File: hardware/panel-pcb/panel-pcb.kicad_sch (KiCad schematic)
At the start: 134 parts, among them J1 USB_C_Receptacle_USB2.0_16P, J10 RS-485 OUT, J11 12V_OUT, J2 SWD, J3 FSR North, J4 FSR East, J5 12V_IN, J6 FSR South, J7 FSR West, J8 RS-485 IN, J9 INT OUT, SW1 PANEL_ID, SW2 BOOTSEL, SW3 RS-485 Termination, U1 RP2040, U2 THVD1419, U3 W25Q32JV, U4 SN74AHCT125, U5 AMS1117-5.0, U6 AP7361C-33ER-13, U7 USBLC6-2SC6, X1 12MHz ABM8-272-T3

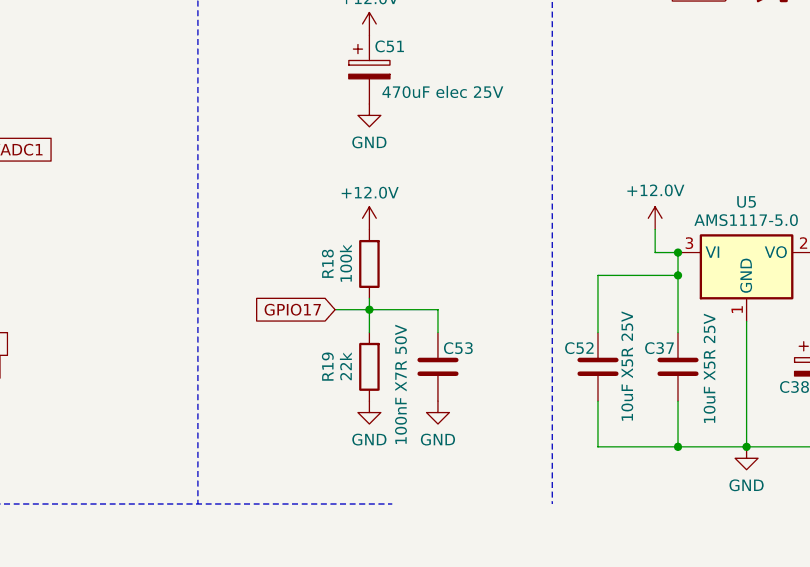
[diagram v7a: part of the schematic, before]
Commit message: Panel PCB: board art, name/rev silk, follow-up review fixes
- Silkscreen: 'Kraken Pad by SenPi / Rev. 1.0' (F.Silk), JLC order-number
  placeholder JLCJLCJLCJLC (B.Silk).
- Personal logo as exposed copper: 5 poly pairs F.Cu + point-registered
  F.Mask openings; degenerate near-zero-area sliver pair deleted
  (follow-up review F3).
- R19 22k -> 33k: 12V-sense node ~2.98V, ~1V margin over guaranteed
  2.0V VIH (follow-up review F1; old 22k value had 164mV nominal margin).
- New D29 PMEG3015EH clamp, anode GPIO17 / cathode +3V3: bounds the
  sense node to one Vf above the rail when IOVDD is down, closing the
  RP2040 abs-max-vs-FT-description ambiguity (follow-up review F2).
- Via DRC rules switched to JLC 4-layer standard class (0.3mm drill /
  0.45mm dia) - board passes clean, no premium via process needed.

ERC: 1 warning (D29 cached D_Schottky lib_symbol_mismatch, known noise
class). DRC 0 violations, 0 unconnected.
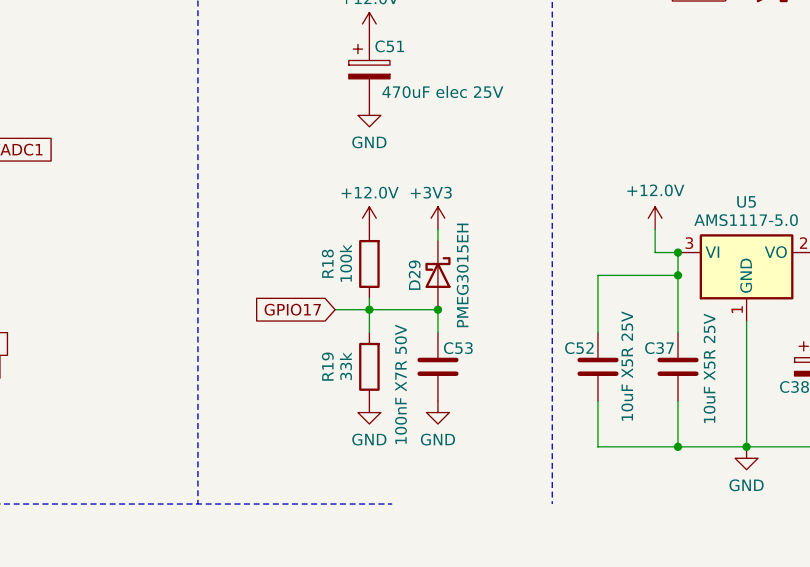
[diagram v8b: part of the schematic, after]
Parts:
- added D29: PMEG3015EH, Diode_SMD:D_SOD-123F, symbol Device:D_Schottky
- R19: value 22k -> 33k
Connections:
- net +3V3: now also D29.1 (K)
- net GPIO17: now also D29.2 (A)
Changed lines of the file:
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@@
 	)
 	(junction
+		(at 304.8 231.14)
+		(diameter 0)
+		(color 0 0 0 0)
+	)
+	(junction
 		(at 92.71 137.16)
 		(diameter 0)
@@
 	(wire
 		(pts
+			(xy 304.8 222.25) (xy 304.8 223.52)
+		)
+		(stroke
+			(width 0)
+			(type default)
+		)
+	)
+	(wire
+		(pts
 			(xy 49.53 138.43) (xy 41.91 138.43)
 		)
@@
 	(symbol
 		(lib_id "power:+3V3")
+		(at 304.8 222.25 0)
+		(unit 1)
+		(body_style 1)
+		(exclude_from_sim no)
+		(in_bom yes)
+		(on_board yes)
+		(in_pos_files yes)
+		(dnp no)
+		(property "Reference" "#PWR0158"
+			(at 304.8 218.44 0)
+			(hide yes)
+			(show_name no)
+			(do_not_autoplace no)
+			(effects
+				(font
+					(size 1.27 1.27)
+				)
+			)
+		)
+		(property "Value" "+3V3"
+			(at 304.038 218.186 0)
+			(show_name no)
+			(do_not_autoplace no)
+			(effects
+				(font
+					(size 1.27 1.27)
+				)
+			)
+		)
+		(property "Footprint" ""
+			(at 304.8 222.25 0)
+			(hide yes)
+			(show_name no)
+			(do_not_autoplace no)
+			(effects
+				(font
+					(size 1.27 1.27)
+				)
+			)
+		)
+		(property "Datasheet" ""
+			(at 304.8 222.25 0)
+			(hide yes)
+			(show_name no)
+			(do_not_autoplace no)
+			(effects
+				(font
+					(size 1.27 1.27)
+				)
+			)
+		)
+		(property "Description" ""
+			(at 304.8 222.25 0)
+			(hide yes)
+			(show_name no)
+			(do_not_autoplace no)
+			(effects
+				(font
+					(size 1.27 1.27)
+				)
+			)
+		)
+		(pin "1"
+		)
+		(instances
+			(project "panel-pcb"
+				(path "/a1b2c3d4-0000-4000-8000-000000000001"
+					(reference "#PWR0158")
+					(unit 1)
+				)
+			)
+		)
+	)
+	(symbol
+		(lib_id "power:+3V3")
 		(at 309.88 31.75 0)
 		(unit 1)
@@
 	)
 	(symbol
+		(lib_id "Device:D_Schottky")
+		(at 304.8 227.33 270)
+		(unit 1)
+		(body_style 1)
+		(exclude_from_sim no)
+		(in_bom yes)
+		(on_board yes)
+		(in_pos_files yes)
+		(dnp no)
+		(property "Reference" "D29"
+			(at 302.26 227.33 0)
+			(show_name no)
+			(do_not_autoplace no)
+			(effects
+				(font
+					(size 1.27 1.27)
+				)
+			)
+		)
+		(property "Value" "PMEG3015EH"
+			(at 307.594 227.33 0)
+			(show_name no)
+			(do_not_autoplace no)
+			(effects
+				(font
+					(size 1.27 1.27)
+				)
+			)
+		)
+		(property "Footprint" "Diode_SMD:D_SOD-123F"
+			(at 299.72 227.33 0)
+			(hide yes)
+			(show_name no)
+			(do_not_autoplace no)
+			(effects
+				(font
+					(size 1.27 1.27)
+				)
+			)
+		)
+		(property "Datasheet" "https://assets.nexperia.com/documents/data-sheet/PMEG3015EH.pdf"
+			(at 299.72 227.33 0)
+			(hide yes)
+			(show_name no)
+			(do_not_autoplace no)
+			(effects
+				(font
+					(size 1.27 1.27)
+				)
+			)
+		)
+		(property "Description" "GPIO17 12V-sense clamp to +3V3\""
+			(at 299.72 227.33 0)
+			(hide yes)
+			(show_name no)
+			(do_not_autoplace no)
+			(effects
+				(font
+					(size 1.27 1.27)
+				)
+			)
+		)
+		(pin "1"
+		)
+		(pin "2"
+		)
+		(instances
+			(project "panel-pcb"
+				(path "/a1b2c3d4-0000-4000-8000-000000000001"
+					(reference "D29")
+					(unit 1)
+				)
+			)
+		)
+	)
+	(symbol
 		(lib_id "Device:C")
 		(at 71.12 144.78 0)
@@
 			)
 		)
-		(property "Value" "22k"
+		(property "Value" "33k"
 			(at 294.64 237.49 90)
 			(show_name no)
